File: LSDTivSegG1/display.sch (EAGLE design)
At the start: 99 parts, among them IC1 MEGA8-P, IC2 MAX232, IC3 PCF8574P, IC4 PCF8574P, IC5 PCF8574P, IC6 PCF8574P

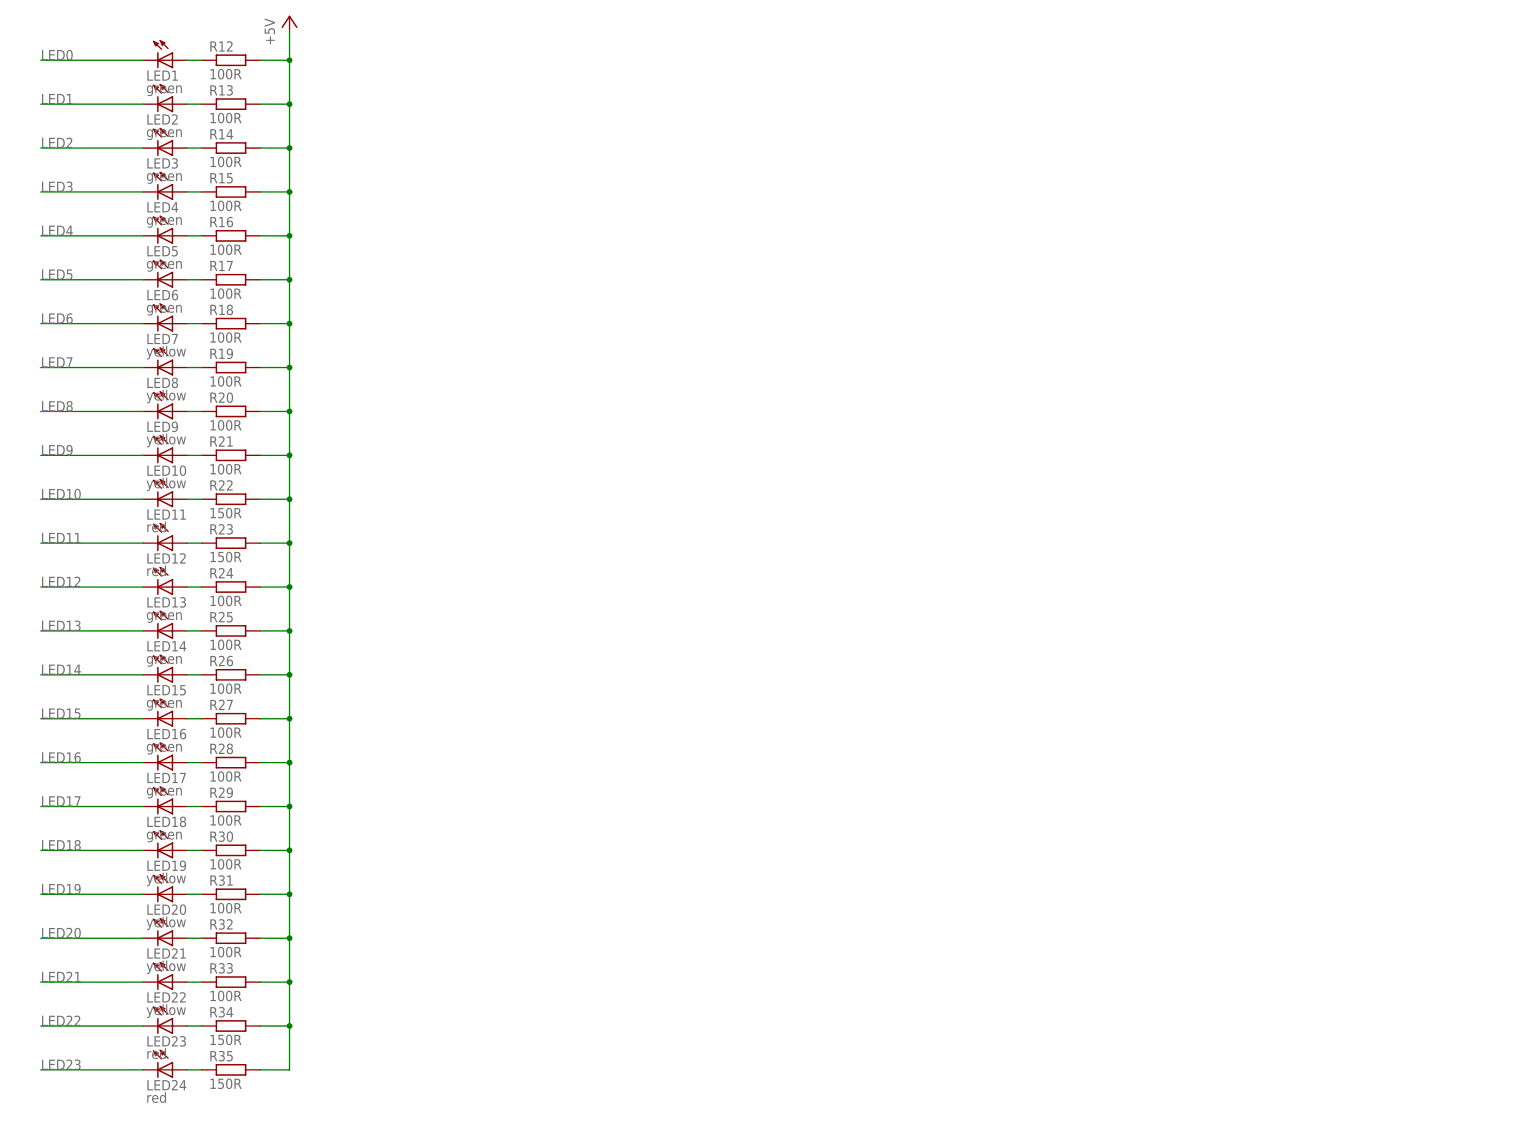
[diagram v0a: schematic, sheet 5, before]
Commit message: added npn transistors to LED bars
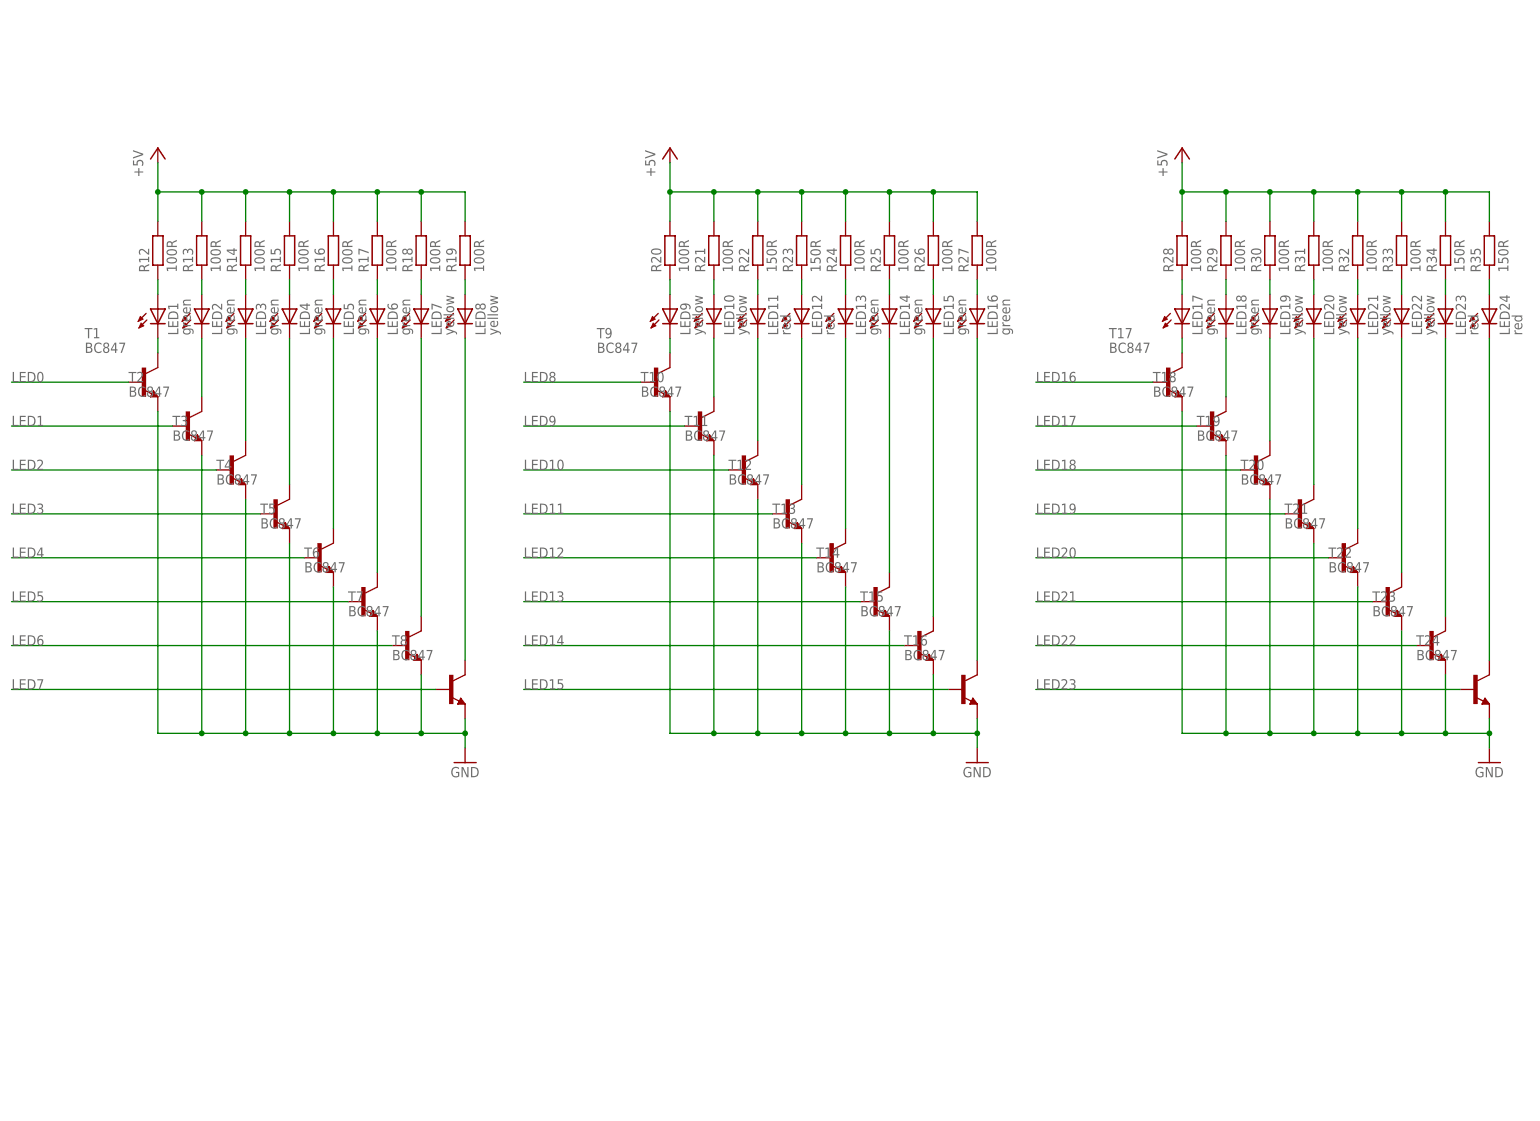
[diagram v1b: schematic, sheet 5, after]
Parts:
- added T1, T10, T11, T12, T13, T14, T15, T16, T17, T18, T19, T2, T20, T21, T22, T23, T24, T3, T4, T5, T6, T7, T8, T9: BC847, transistor:BC847
- LED17, LED20, LED21, LED22, LED23, LED24: SPICEPREFIX (none) -> L
- LED18: SPICEPREFIX (none) -> X
- LED19: SPICEPREFIX (none) -> B
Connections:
- new net N$51: LED9.C, T9.C
- new net N$53: LED1.C, T1.C
- new net N$54: LED2.C, T2.C
- new net N$55: LED3.C, T3.C
- new net N$56: LED4.C, T4.C
- new net N$57: LED5.C, T5.C
- new net N$58: LED6.C, T6.C
- new net N$59: LED17.C, T17.C
- new net N$60: LED10.C, T10.C
- new net N$61: LED11.C, T11.C
- new net N$62: LED12.C, T12.C
- new net N$63: LED13.C, T13.C
- new net N$64: LED14.C, T14.C
- new net N$65: LED7.C, T7.C
- new net N$66: LED8.C, T8.C
- new net N$67: LED15.C, T15.C
- new net N$68: LED16.C, T16.C
- new net N$69: LED18.C, T18.C
- new net N$70: LED19.C, T19.C
- new net N$71: LED20.C, T20.C
- new net N$72: LED21.C, T21.C
- new net N$73: LED22.C, T22.C
- new net N$74: LED23.C, T23.C
- new net N$75: LED24.C, T24.C
- net GND: now also T1.E, T10.E, T11.E, T12.E, T13.E, T14.E, T15.E, T16.E, T17.E, T18.E, T19.E, T2.E, T20.E, T21.E, T22.E, T23.E, T24.E, T3.E, T4.E, T5.E, T6.E, T7.E, T8.E, T9.E
- net LED0: now also T1.B; no longer LED1.C
- net LED1: now also T2.B; no longer LED2.C
- net LED10: now also T11.B; no longer LED11.C
- net LED11: now also T12.B; no longer LED12.C
- net LED12: now also T13.B; no longer LED13.C
- net LED13: now also T14.B; no longer LED14.C
- net LED14: now also T15.B; no longer LED15.C
- net LED15: now also T16.B; no longer LED16.C
- net LED16: now also T17.B; no longer LED17.C
- net LED17: now also T18.B; no longer LED18.C
- net LED18: now also T19.B; no longer LED19.C
- net LED19: now also T20.B; no longer LED20.C
- net LED2: now also T3.B; no longer LED3.C
- net LED20: now also T21.B; no longer LED21.C
- net LED21: now also T22.B; no longer LED22.C
- net LED22: now also T23.B; no longer LED23.C
- net LED23: now also T24.B; no longer LED24.C
- net LED3: now also T4.B; no longer LED4.C
- net LED4: now also T5.B; no longer LED5.C
- net LED5: now also T6.B; no longer LED6.C
- net LED6: now also T7.B; no longer LED7.C
- net LED7: now also T8.B; no longer LED8.C
- net LED8: now also T9.B; no longer LED9.C
- net LED9: now also T10.B; no longer LED10.C
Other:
- moved on the sheet: LED1, LED10, LED11, LED12, LED13, LED14, LED15, LED16, LED17, LED18, LED19, LED2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

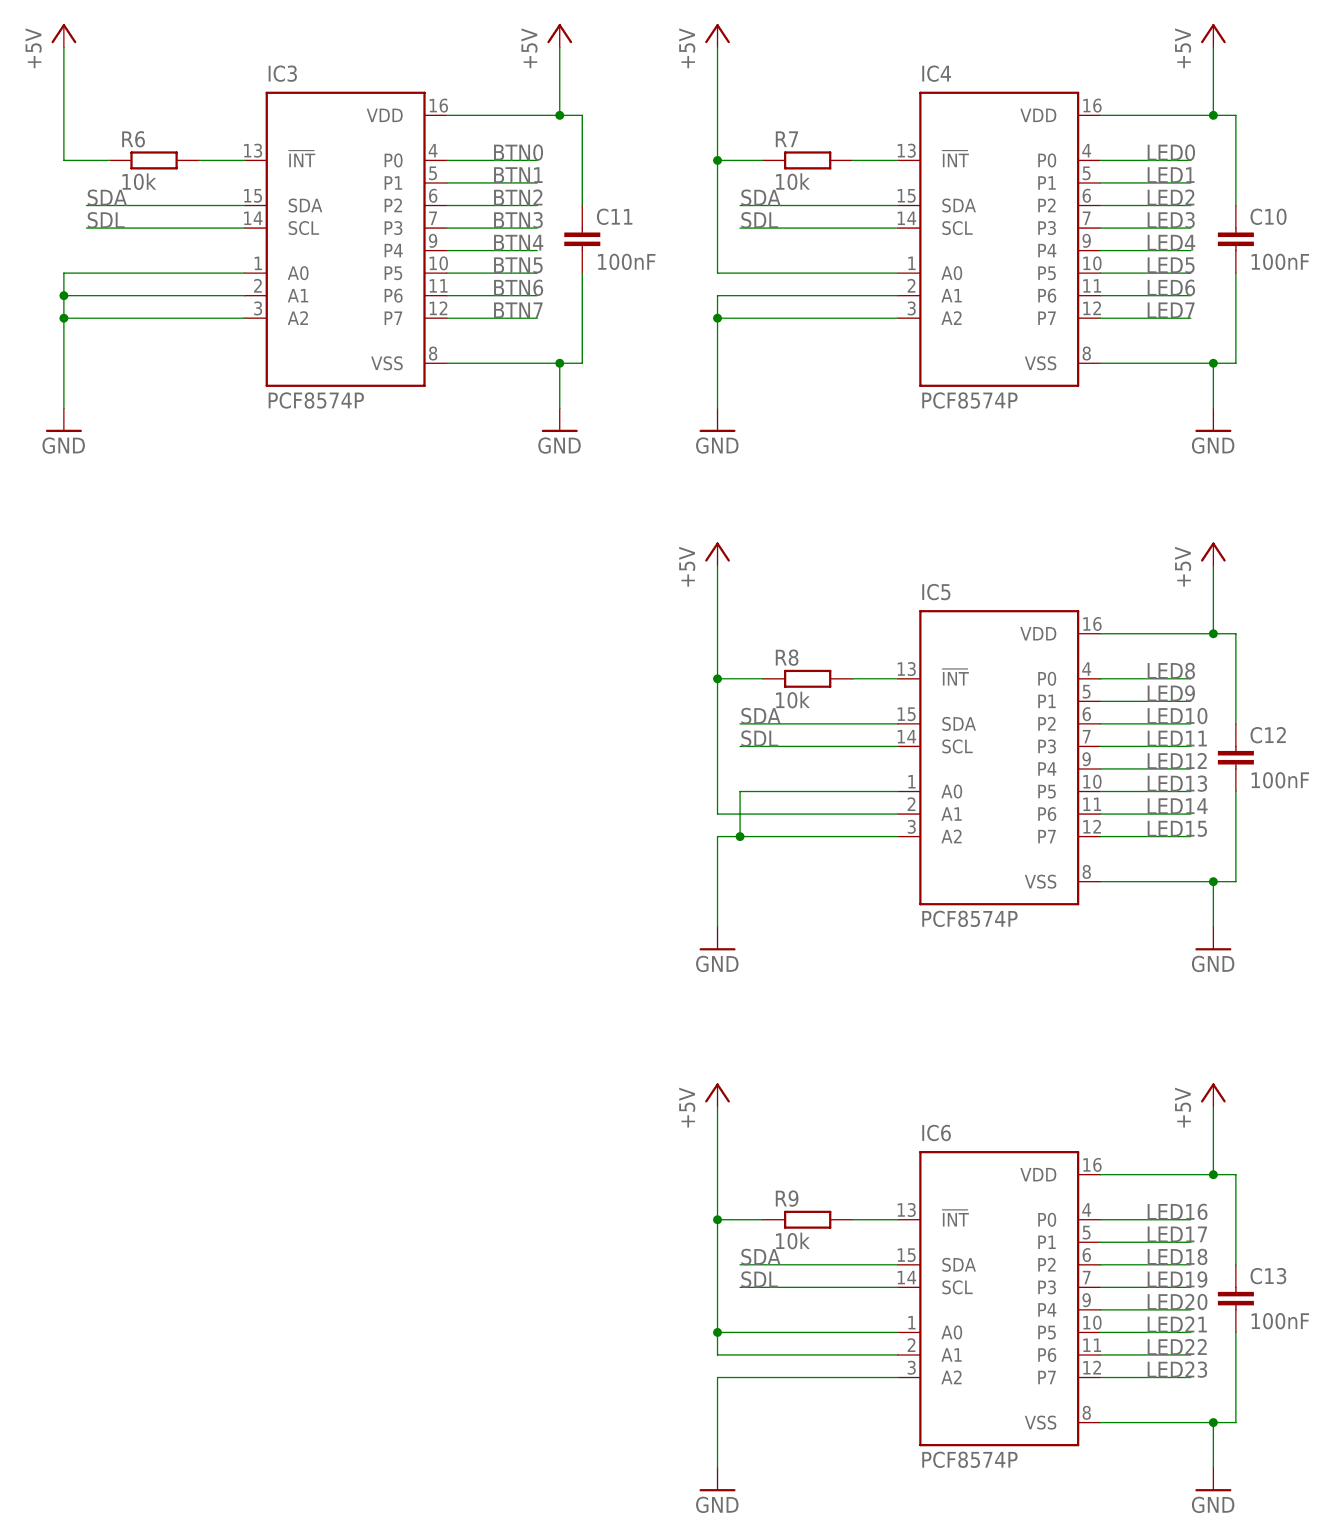
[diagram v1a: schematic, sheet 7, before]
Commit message: fixed wrong naming of SCL (used SDL) for IO-Expanders
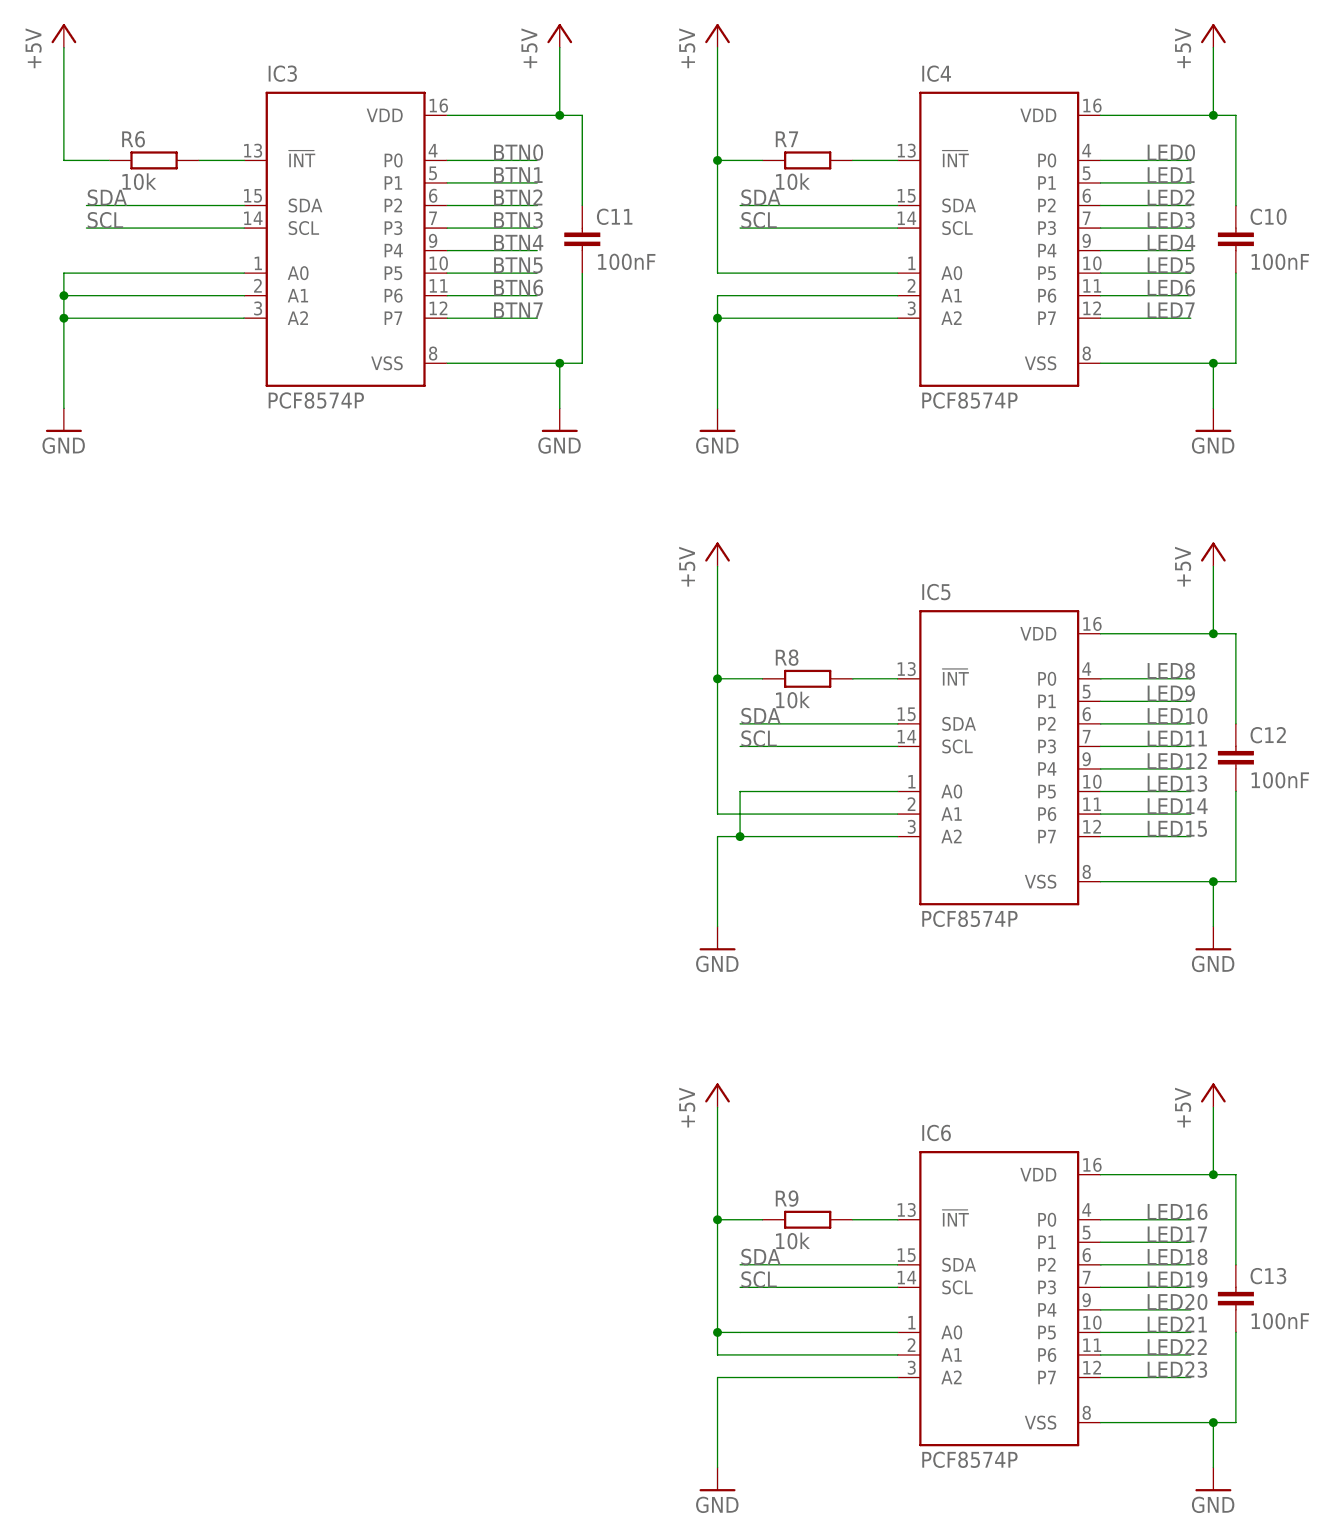
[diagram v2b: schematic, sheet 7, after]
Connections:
- removed net SDL: IC3.SCL, IC4.SCL, IC5.SCL, IC6.SCL
- net SCL: now also IC3.SCL, IC4.SCL, IC5.SCL, IC6.SCL
